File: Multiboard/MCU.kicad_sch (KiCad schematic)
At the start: 47 parts, among them J1 Conn_01x20_Socket, J2 Conn_01x20_Socket, J3 Debug, J4 USB_C_Receptacle_USB2.0_16P, SW1 BOOT0, SW2 NRST, SW7 KEY, U1 STM32F411RET6, U2 MAX662AESA_T, U3 MCP1792x-3302xCB, Y1 32.768KHz, Y2 25MHz

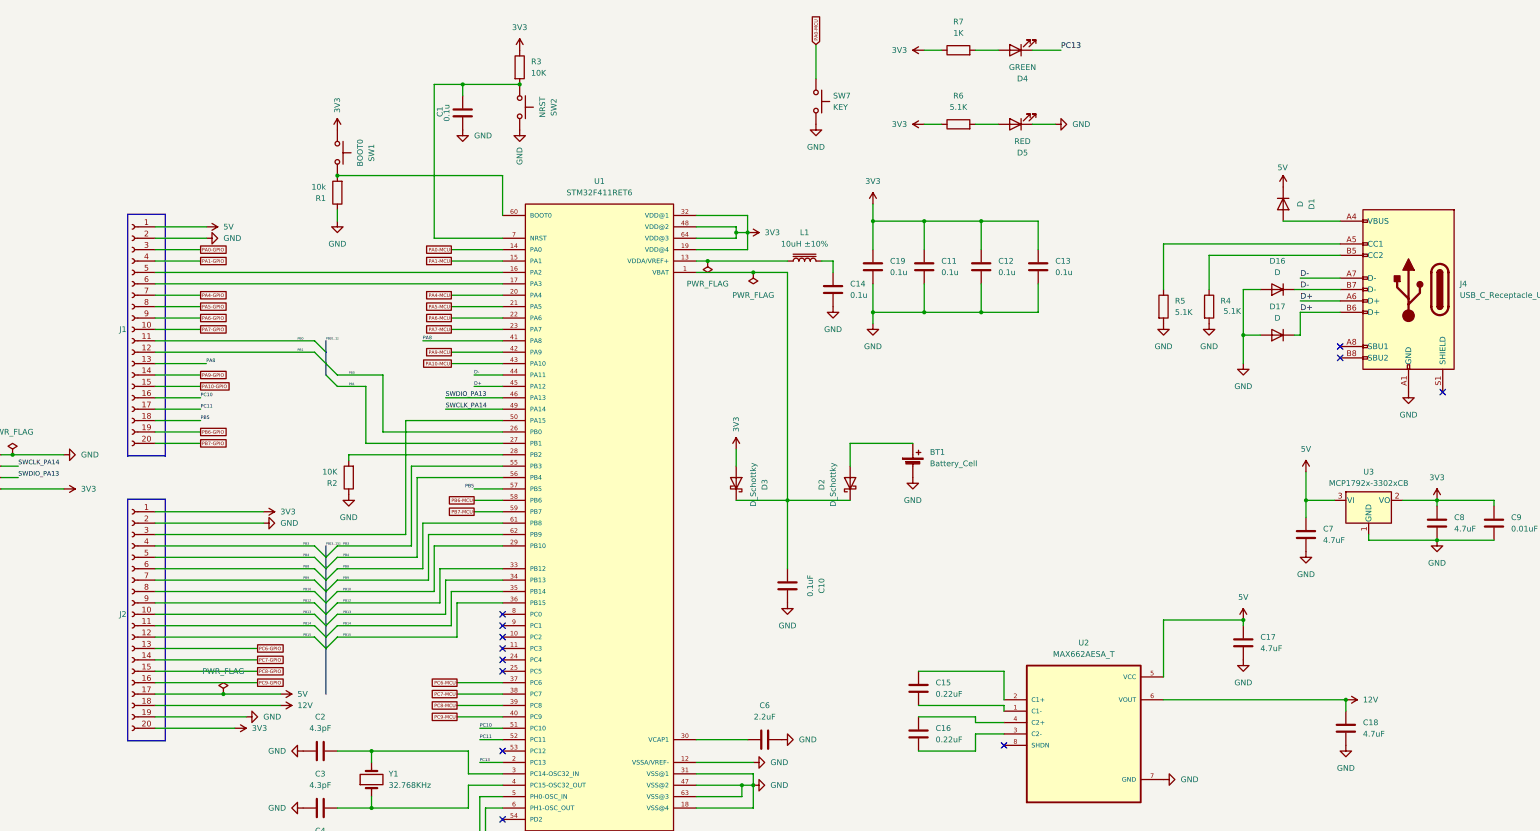
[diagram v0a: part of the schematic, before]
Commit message: fixed dead copper zones and cleared all errors
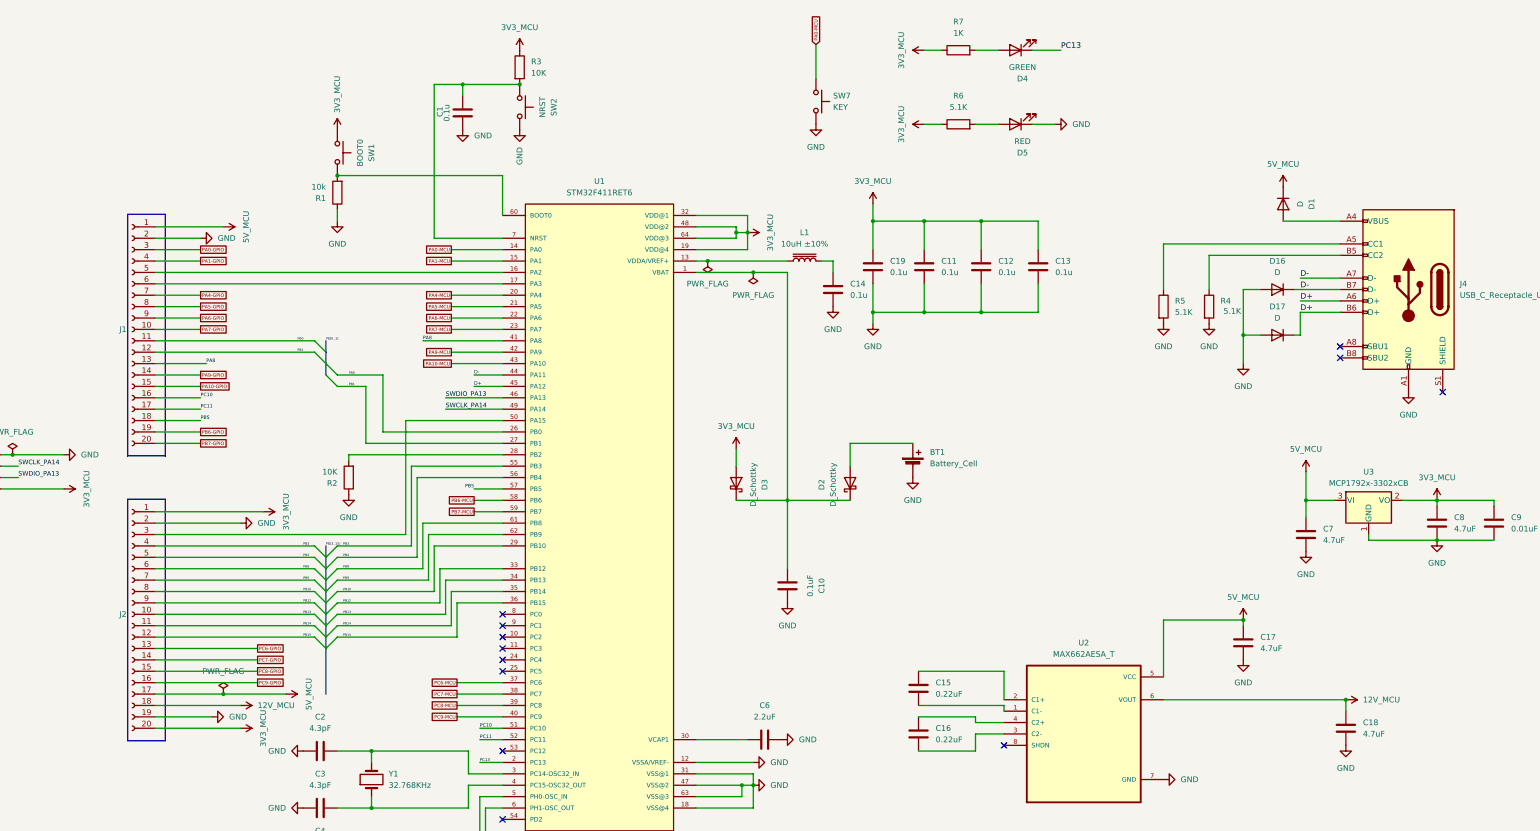
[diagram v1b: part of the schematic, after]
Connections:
- net 12V renamed 12V_MCU
- net 3V3 renamed 3V3_MCU
- net 5V renamed 5V_MCU

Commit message: added top layer copper zone with stitiching vias,  fixed trace issues and changed mcu pins footprint
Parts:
- J1, J2: footprint Connector_JST:JST_XA_B20B-XASK-1-A_1x20_P2.50mm_Vertical -> Connector_PinHeader_2.54mm:PinHeader_1x20_P2.54mm_Vertical
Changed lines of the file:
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@@
 			)
 		)
-		(property "Footprint" "Connector_JST:JST_XA_B20B-XASK-1-A_1x20_P2.50mm_Vertical"
+		(property "Footprint" "Connector_PinHeader_2.54mm:PinHeader_1x20_P2.54mm_Vertical"
 			(at 73.66 148.59 0)
 			(effects
@@
 			)
 		)
-		(property "Footprint" "Connector_JST:JST_XA_B20B-XASK-1-A_1x20_P2.50mm_Vertical"
+		(property "Footprint" "Connector_PinHeader_2.54mm:PinHeader_1x20_P2.54mm_Vertical"
 			(at 73.66 85.09 0)
 			(effects

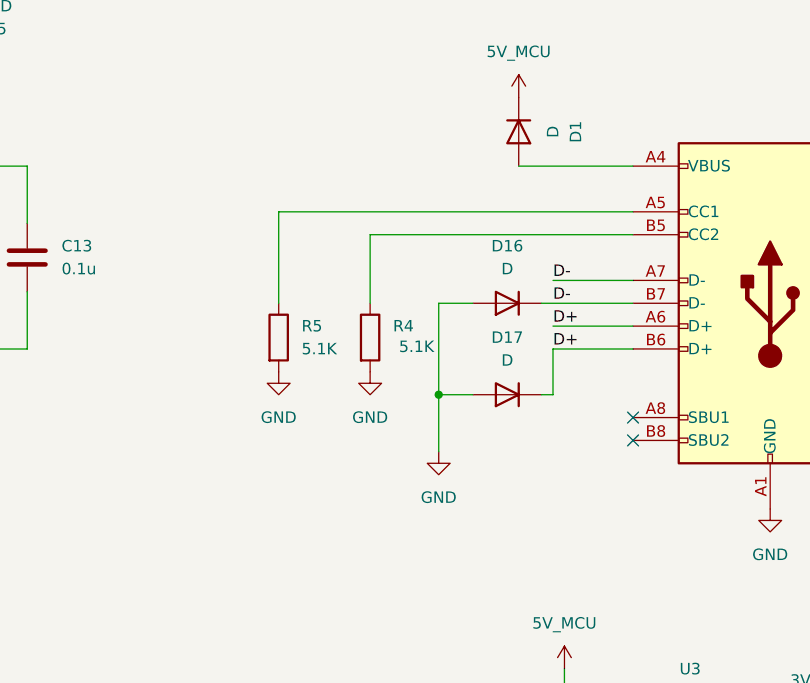
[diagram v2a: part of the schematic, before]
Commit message: fixed missing fpga pins and added dedicated usb protection ic instead of diodes
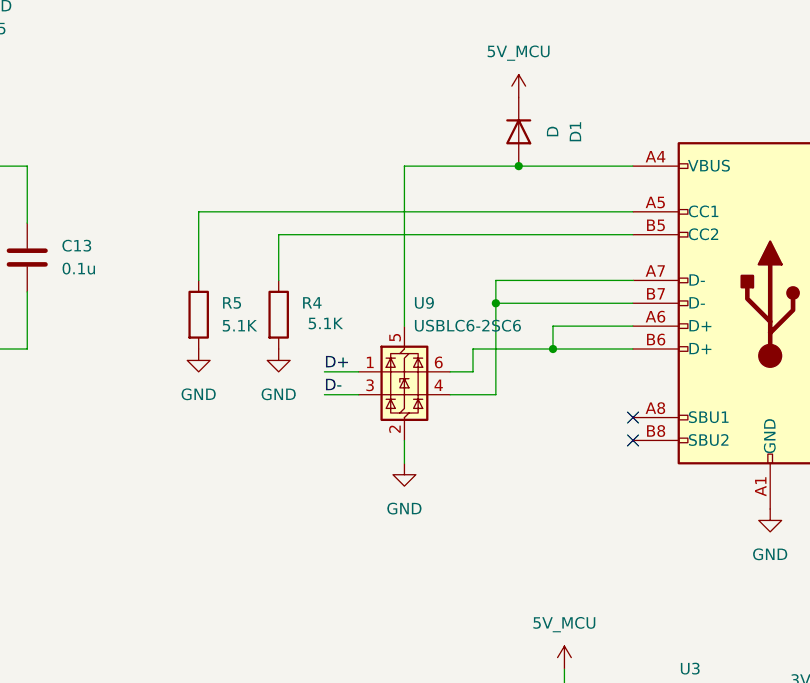
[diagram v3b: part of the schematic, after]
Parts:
- removed D16, D17: D, Diode_SMD:D_0603_1608Metric_Pad1.05x0.95mm_HandSolder, symbol Device:D
- added U9: USBLC6-2SC6, Package_TO_SOT_SMD:SOT-23-6, symbol Power_Protection:USBLC6-2SC6
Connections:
- net D+: now also U9.1 (I/O1); no longer J4.A6 (D+), J4.B6 (D+)
- net D-: now also U9.3 (I/O2); no longer J4.A7 (D-), J4.B7 (D-)
- net GND: now also U9.2 (GND)
- net at D1.2 (A), J4.A4 (VBUS), J4.A9 (VBUS)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: now also U9.5 (VBUS)
- new net: J4.A7 (D-), J4.B7 (D-), U9.4 (I/O2)
- new net: J4.A6 (D+), J4.B6 (D+), U9.6 (I/O1)
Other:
- moved on the sheet: R4, R5

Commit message: Generated BOM
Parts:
- removed U3: MCP1792x-3302xCB, Package_TO_SOT_SMD:SOT-23, symbol Regulator_Linear:MCP1792x-3302xCB
- added U3: ME6211C33M5, Package_TO_SOT_SMD:SOT-23-5, symbol Regulator_Linear:ME6211C33M5
- C1, C10, C11, C12, C13, C14, C19: LCSC Part Number (none) -> C14663
- C15, C16: LCSC Part Number (none) -> C64705
- C17, C7, C8: LCSC Part Number (none) -> C19666
- C18: LCSC Part Number (none) -> C161217
- C2, C3: LCSC Part Number (none) -> C519375
- C4, C5: LCSC Part Number (none) -> C38523
- C6: LCSC Part Number (none) -> C913904
- C9: LCSC Part Number (none) -> C100042
- D2, D3: footprint Diode_SMD:D_0603_1608Metric_Pad1.05x0.95mm_HandSolder -> Diode_SMD:D_SOD-323F; LCSC Part Number (none) -> C2903903
- D4: LCSC Part Number (none) -> C2994781
- D5: LCSC Part Number (none) -> C2846640
- J4: LCSC Part Number (none) -> C2988369
- L1: LCSC Part Number (none) -> C6808014
- R1, R2, R3: LCSC Part Number (none) -> C98220
- R4, R5, R6: LCSC Part Number (none) -> C2907044
- R7: LCSC Part Number (none) -> C22548
- SW1, SW2, SW7: LCSC Part Number (none) -> C7528752
- U1: LCSC Part Number (none) -> C94355
- U2: LCSC Part Number (none) -> C2976348
- U9: LCSC Part Number (none) -> C7519
- Y1: LCSC Part Number (none) -> C95361
- Y2: LCSC Part Number (none) -> C255920
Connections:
- net 3V3_MCU: now also U3.5 (V_{OUT})
- net 5V_MCU: now also U3.1 (V_{IN}), U3.3 (CE)
- net GND: now also U3.2 (V_{SS})
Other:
- moved on the sheet: C11, C12, C13, C19

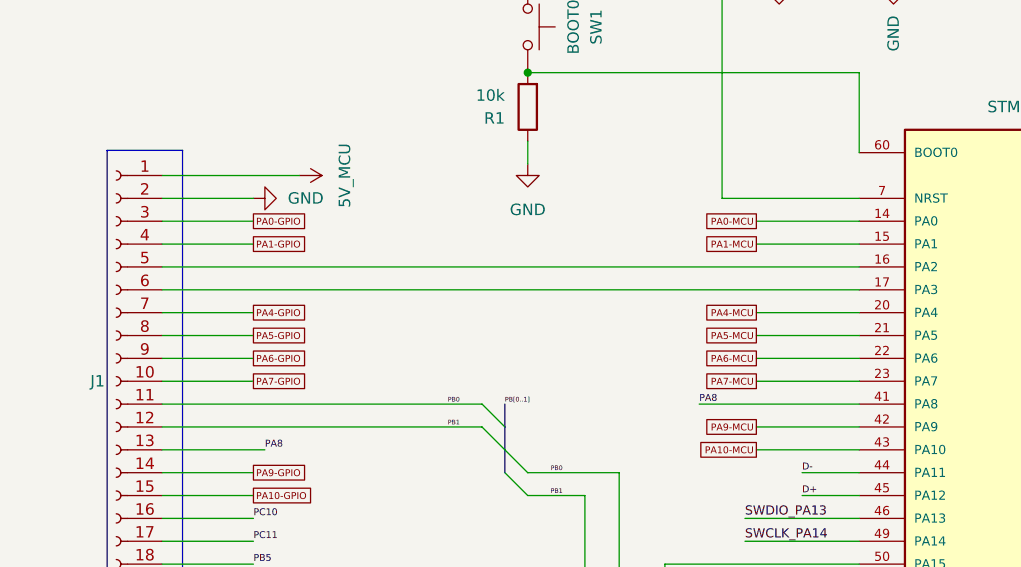
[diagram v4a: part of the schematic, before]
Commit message: fixed MCU LDO
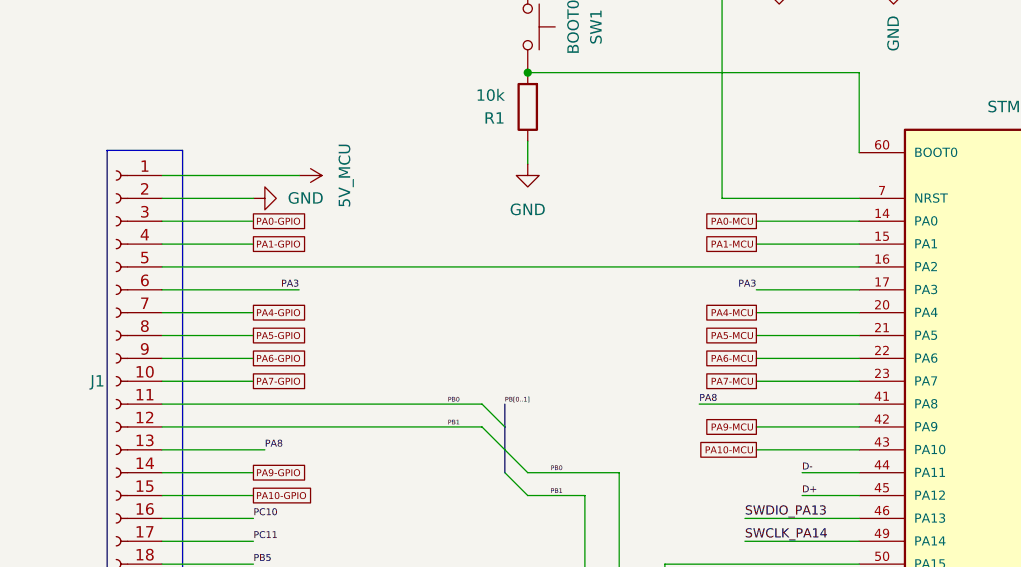
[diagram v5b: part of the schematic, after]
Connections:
- net PA3: now reaches J1.6 (Pin_6), U1.17 (PA3)
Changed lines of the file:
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@@
+	(wire
+		(pts
+			(xy 144.78 74.93) (xy 156.21 74.93)
+		)
+		(stroke
+			(width 0)
+			(type default)
+		)
+	)
 	(wire
 		(pts
@@
 	(wire
 		(pts
+			(xy 78.74 74.93) (xy 93.98 74.93)
+		)
+		(stroke
+			(width 0)
+			(type default)
+		)
+	)
+	(wire
+		(pts
 			(xy 335.28 116.84) (xy 335.28 123.19)
-		)
-		(stroke
-			(width 0)
-			(type default)
-		)
-	)
-	(wire
-		(pts
-			(xy 78.74 74.93) (xy 156.21 74.93)
 		)
 		(stroke
@@
 		)
 	)
+	(label "PA3"
+		(at 93.98 74.93 180)
+		(effects
+			(font
+				(size 0.762 0.762)
+			)
+			(justify right bottom)
+		)
+	)
 	(label "PB12"
 		(at 120.65 146.05 0)
@@
 		)
 	)
+	(label "PA3"
+		(at 144.78 74.93 180)
+		(effects
+			(font
+				(size 0.762 0.762)
+			)
+			(justify right bottom)
+		)
+	)
